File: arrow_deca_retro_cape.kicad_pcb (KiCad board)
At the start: 2 copper layers, 100 x 100 mm, 78 parts, among them J1 DB15_Female_HighDensity_Mount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, J10 Conn_02x06_Odd_Even, J11 PMOD1, J12 PMOD2, J14 Conn_01x02, J15 Conn_01x03, J16 Conn_01x06, J17 Conn_01x02, J18 Conn_01x03, J19 DINC_MIN_TM_6_1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

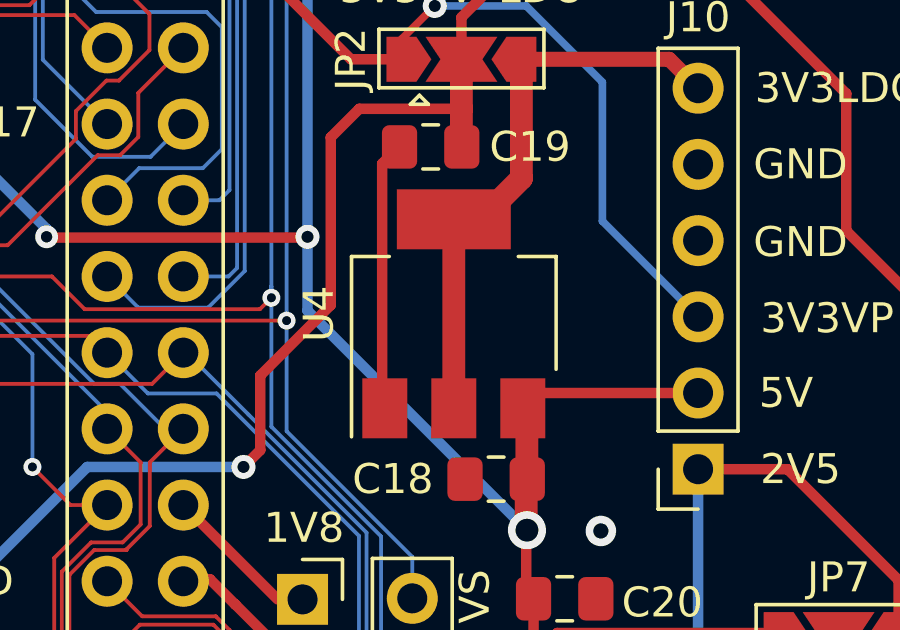
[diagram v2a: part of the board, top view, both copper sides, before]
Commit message: v0.83 Added jlcpcb parts with jlcpcb tools plugin
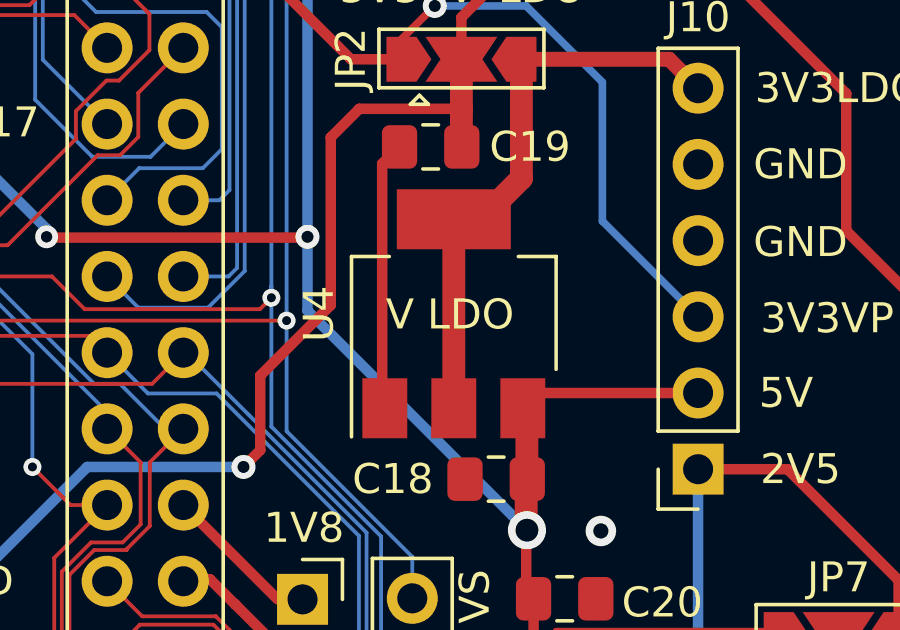
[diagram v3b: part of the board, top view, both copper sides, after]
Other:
- board text added: "V LDO"
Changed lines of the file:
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@@
     (property "Sheetfile" "arrow_deca_retro_cape.kicad_sch")
     (property "Sheetname" "")
-    (attr through_hole)
+    (attr through_hole exclude_from_pos_files exclude_from_bom)
     (fp_text reference "J9" (at 1.283 -2.9718 180) (layer "F.SilkS")
       (effects (font (size 1 1) (thickness 0.15)))
@@
     (property "Sheetfile" "arrow_deca_retro_cape.kicad_sch")
     (property "Sheetname" "")
-    (attr through_hole)
+    (attr through_hole exclude_from_pos_files exclude_from_bom)
     (fp_text reference "J8" (at 1.156 -2.9718) (layer "F.SilkS")
       (effects (font (size 1 1) (thickness 0.15)))
@@
     (property "Sheetfile" "arrow_deca_retro_cape.kicad_sch")
     (property "Sheetname" "")
-    (attr smd)
+    (attr smd exclude_from_pos_files exclude_from_bom)
     (fp_text reference "U4" (at 0 -4.5 90) (layer "F.SilkS")
       (effects (font (size 1 1) (thickness 0.15)))
@@
     (property "Sheetfile" "arrow_deca_retro_cape.kicad_sch")
     (property "Sheetname" "")
-    (attr through_hole)
+    (attr through_hole exclude_from_pos_files exclude_from_bom)
     (fp_text reference "J20" (at -0.923331 15.315 -180) (layer "F.SilkS") hide
       (effects (font (size 1 1) (thickness 0.15)))
@@
     (property "Sheetfile" "arrow_deca_retro_cape.kicad_sch")
     (property "Sheetname" "")
-    (attr through_hole)
+    (attr through_hole exclude_from_pos_files exclude_from_bom)
     (fp_text reference "JP5" (at 0 -2.33) (layer "F.SilkS")
       (effects (font (size 1 1) (thickness 0.15)))
@@
     (property "Sheetfile" "arrow_deca_retro_cape.kicad_sch")
     (property "Sheetname" "")
-    (attr through_hole)
+    (attr through_hole exclude_from_pos_files exclude_from_bom)
     (fp_text reference "J2" (at 0 -2.286 180) (layer "F.SilkS")
       (effects (font (size 1 1) (thickness 0.15)))
@@
     (property "Sheetfile" "arrow_deca_retro_cape.kicad_sch")
     (property "Sheetname" "")
-    (attr through_hole)
+    (attr through_hole exclude_from_pos_files exclude_from_bom)
     (fp_text reference "J16" (at 0 -2.77 180) (layer "F.SilkS")
       (effects (font (size 1 1) (thickness 0.15)))
@@
     (property "Sheetfile" "arrow_deca_retro_cape.kicad_sch")
     (property "Sheetname" "")
-    (attr exclude_from_pos_files)
+    (attr exclude_from_pos_files exclude_from_bom)
     (fp_text reference "JP2" (at -3.683 0 90) (layer "F.SilkS")
       (effects (font (size 1 1) (thickness 0.15)))
@@
     (property "Sheetfile" "arrow_deca_retro_cape.kicad_sch")
     (property "Sheetname" "")
-    (attr through_hole)
+    (attr through_hole exclude_from_pos_files exclude_from_bom)
     (fp_text reference "JP8" (at 0 -2.33 90) (layer "F.SilkS")
       (effects (font (size 1 1) (thickness 0.15)))
@@
     (property "Sheetfile" "arrow_deca_retro_cape.kicad_sch")
     (property "Sheetname" "")
-    (attr smd)
+    (attr smd exclude_from_pos_files exclude_from_bom)
     (fp_text reference "R3" (at -2.908 0) (layer "F.SilkS")
       (effects (font (size 1 1) (thickness 0.15)))
@@
     (property "Sheetfile" "arrow_deca_retro_cape.kicad_sch")
     (property "Sheetname" "")
-    (attr through_hole)
+    (attr through_hole exclude_from_pos_files exclude_from_bom)
     (fp_text reference "J10" (at 0 15.061 180) (layer "F.SilkS")
       (effects (font (size 1 1) (thickness 0.15)))
@@
     (property "Sheetfile" "arrow_deca_retro_cape.kicad_sch")
     (property "Sheetname" "")
-    (attr through_hole)
+    (attr through_hole exclude_from_pos_files exclude_from_bom)
     (fp_text reference "J11" (at -1.27 -2.77 90) (layer "F.SilkS") hide
       (effects (font (size 1 1) (thickness 0.15)))
@@
     (property "Sheetfile" "arrow_deca_retro_cape.kicad_sch")
     (property "Sheetname" "")
-    (attr through_hole)
+    (attr through_hole exclude_from_pos_files exclude_from_bom)
     (fp_text reference "JP4" (at 0 -2.33) (layer "F.SilkS")
       (effects (font (size 1 1) (thickness 0.15)))
@@
     (property "Sheetfile" "arrow_deca_retro_cape.kicad_sch")
     (property "Sheetname" "")
+    (attr exclude_from_pos_files exclude_from_bom)
     (fp_text reference "J5" (at -7.5596 12.827 90) (layer "F.SilkS")
       (effects (font (size 1 1) (thickness 0.15)) (justify left bottom))
@@
     (property "Sheetfile" "arrow_deca_retro_cape.kicad_sch")
     (property "Sheetname" "")
-    (attr exclude_from_pos_files)
+    (attr exclude_from_pos_files exclude_from_bom)
     (fp_text reference "JP3" (at -0.142 2.032 90 unlocked) (layer "F.SilkS")
       (effects (font (size 1 1) (thickness 0.15)))
@@
     (property "Sheetfile" "arrow_deca_retro_cape.kicad_sch")
     (property "Sheetname" "")
-    (attr through_hole)
+    (attr through_hole exclude_from_pos_files exclude_from_bom)
     (fp_text reference "J1" (at -4.315 -2.61 -90) (layer "F.SilkS") hide
       (effects (font (size 1 1) (thickness 0.15)))
@@
     (property "Sheetfile" "arrow_deca_retro_cape.kicad_sch")
     (property "Sheetname" "")
-    (attr smd)
+    (attr smd exclude_from_pos_files exclude_from_bom)
     (fp_text reference "U5" (at 0.4814 -4.243469 -90) (layer "F.SilkS")
       (effects (font (size 1 1) (thickness 0.15)))
@@
     (property "Sheetfile" "arrow_deca_retro_cape.kicad_sch")
     (property "Sheetname" "")
-    (attr smd)
+    (attr smd exclude_from_pos_files exclude_from_bom)
     (fp_text reference "R4" (at -2.908 0) (layer "F.SilkS")
       (effects (font (size 1 1) (thickness 0.15)))
@@
     (property "Sheetfile" "arrow_deca_retro_cape.kicad_sch")
     (property "Sheetname" "")
-    (attr exclude_from_pos_files)
+    (attr exclude_from_pos_files exclude_from_bom)
     (fp_text reference "JP7" (at 0 -1.905) (layer "F.SilkS")
       (effects (font (size 1 1) (thickness 0.15)))
@@
     (property "Sheetfile" "arrow_deca_retro_cape.kicad_sch")
     (property "Sheetname" "")
-    (attr through_hole)
+    (attr through_hole exclude_from_pos_files exclude_from_bom)
     (fp_text reference "J3" (at -0.0508 -2.286 180) (layer "F.SilkS")
       (effects (font (size 1 1) (thickness 0.15)))
@@
     (property "Sheetfile" "arrow_deca_retro_cape.kicad_sch")
     (property "Sheetname" "")
-    (attr through_hole)
+    (attr through_hole exclude_from_pos_files exclude_from_bom)
     (fp_text reference "J14" (at -0.025 6.33) (layer "F.SilkS")
       (effects (font (size 1 1) (thickness 0.15)))
@@
     (property "Sheetfile" "arrow_deca_retro_cape.kicad_sch")
     (property "Sheetname" "")
+    (attr exclude_from_pos_files exclude_from_bom)
     (fp_text reference "J19" (at -7.5946 12.827 90) (layer "F.SilkS")
       (effects (font (size 1 1) (thickness 0.15)) (justify left bottom))
@@
     (property "Sheetfile" "arrow_deca_retro_cape.kicad_sch")
     (property "Sheetname" "")
-    (attr through_hole)
+    (attr through_hole exclude_from_pos_files exclude_from_bom)
     (fp_text reference "J15" (at 0 -2.33 90) (layer "F.SilkS")
       (effects (font (size 1 1) (thickness 0.15)))
@@
     (property "Sheetfile" "arrow_deca_retro_cape.kicad_sch")
     (property "Sheetname" "")
-    (attr through_hole)
+    (attr through_hole exclude_from_pos_files exclude_from_bom)
     (fp_text reference "J4" (at 22.112 -1.221669) (layer "F.SilkS")
       (effects (font (size 1 1) (thickness 0.15)))
@@
     (property "Sheetfile" "arrow_deca_retro_cape.kicad_sch")
     (property "Sheetname" "")
-    (attr through_hole)
+    (attr through_hole exclude_from_pos_files exclude_from_bom)
     (fp_text reference "J18" (at 0 -2.301) (layer "F.SilkS")
       (effects (font (size 1 1) (thickness 0.15)))
@@
     (property "Sheetfile" "arrow_deca_retro_cape.kicad_sch")
     (property "Sheetname" "")
-    (attr through_hole)
+    (attr through_hole exclude_from_pos_files exclude_from_bom)
     (fp_text reference "JP6" (at 0 -2.33) (layer "F.SilkS")
       (effects (font (size 1 1) (thickness 0.15)))
@@
     (property "Sheetfile" "arrow_deca_retro_cape.kicad_sch")
     (property "Sheetname" "")
-    (attr through_hole)
+    (attr through_hole exclude_from_pos_files exclude_from_bom)
     (fp_text reference "J17" (at 0.0508 6.8326 180) (layer "F.SilkS")
       (effects (font (size 1 1) (thickness 0.15)))
@@
     (property "Sheetfile" "arrow_deca_retro_cape.kicad_sch")
     (property "Sheetname" "")
-    (attr through_hole)
+    (attr through_hole exclude_from_pos_files exclude_from_bom)
     (fp_text reference "J22" (at 0 -2.33) (layer "F.SilkS")
       (effects (font (size 1 1) (thickness 0.15)))
@@
     (property "Sheetfile" "arrow_deca_retro_cape.kicad_sch")
     (property "Sheetname" "")
-    (attr through_hole)
+    (attr through_hole exclude_from_pos_files exclude_from_bom)
     (fp_text reference "J12" (at -1.27 -2.77 90) (layer "F.SilkS") hide
       (effects (font (size 1 1) (thickness 0.15)))
@@
     (property "Sheetfile" "arrow_deca_retro_cape.kicad_sch")
     (property "Sheetname" "")
-    (attr through_hole)
+    (attr through_hole exclude_from_pos_files exclude_from_bom)
     (fp_text reference "JP1" (at -2.159 1.143 -180) (layer "F.SilkS")
       (effects (font (size 1 1) (thickness 0.15)))
@@
     (property "Sheetfile" "arrow_deca_retro_cape.kicad_sch")
     (property "Sheetname" "")
-    (attr through_hole)
+    (attr through_hole exclude_from_pos_files exclude_from_bom)
     (fp_text reference "J7" (at 0 7.685) (layer "F.SilkS")
       (effects (font (size 1 1) (thickness 0.15)))
@@
     (property "Sheetfile" "arrow_deca_retro_cape.kicad_sch")
     (property "Sheetname" "")
-    (attr through_hole)
+    (attr through_hole exclude_from_pos_files exclude_from_bom)
     (fp_text reference "J6" (at 1.27 50.8) (layer "F.SilkS")
       (effects (font (size 1 1) (thickness 0.15)))
@@
     (effects (font (size 1 1) (thickness 0.15)))
   )
+  (gr_text "V LDO" (at 128.27 77.47) (layer "F.SilkS")
+    (effects (font (size 1 1) (thickness 0.15)))
+  )

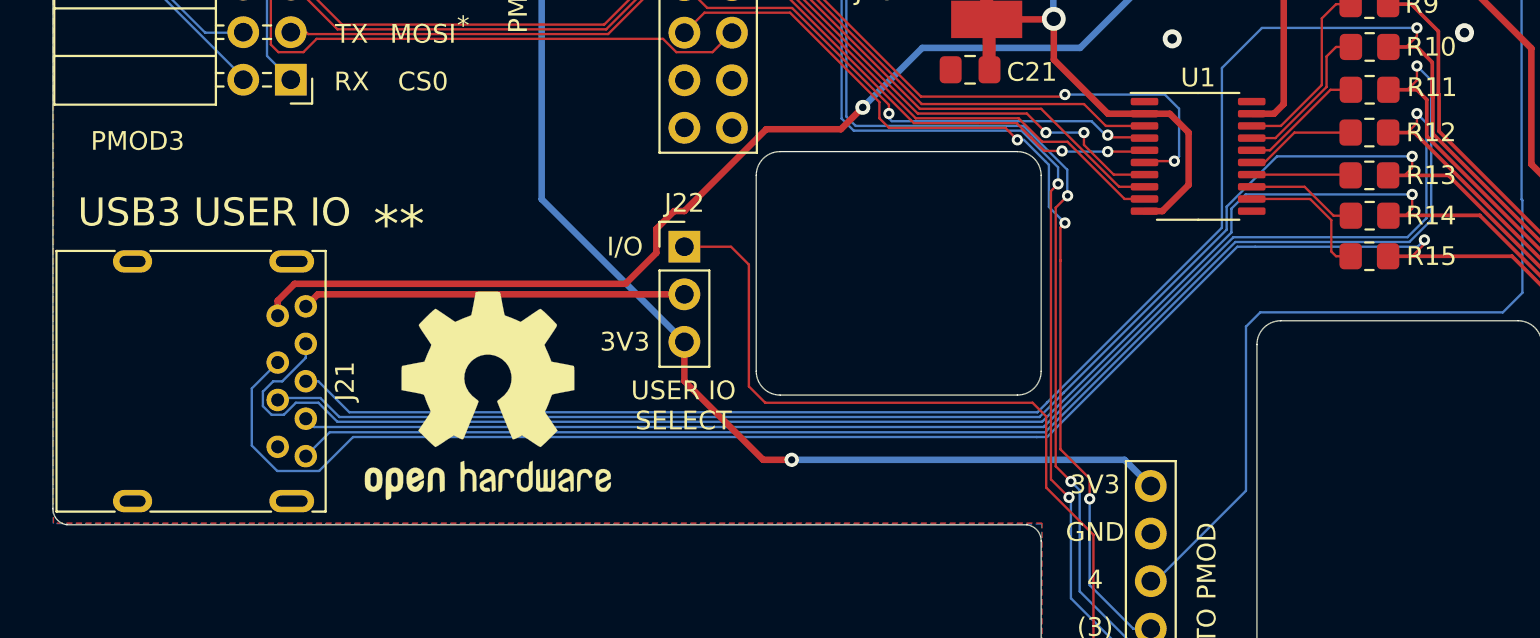
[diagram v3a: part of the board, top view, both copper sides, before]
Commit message: v0.84 updated USB3 footprint
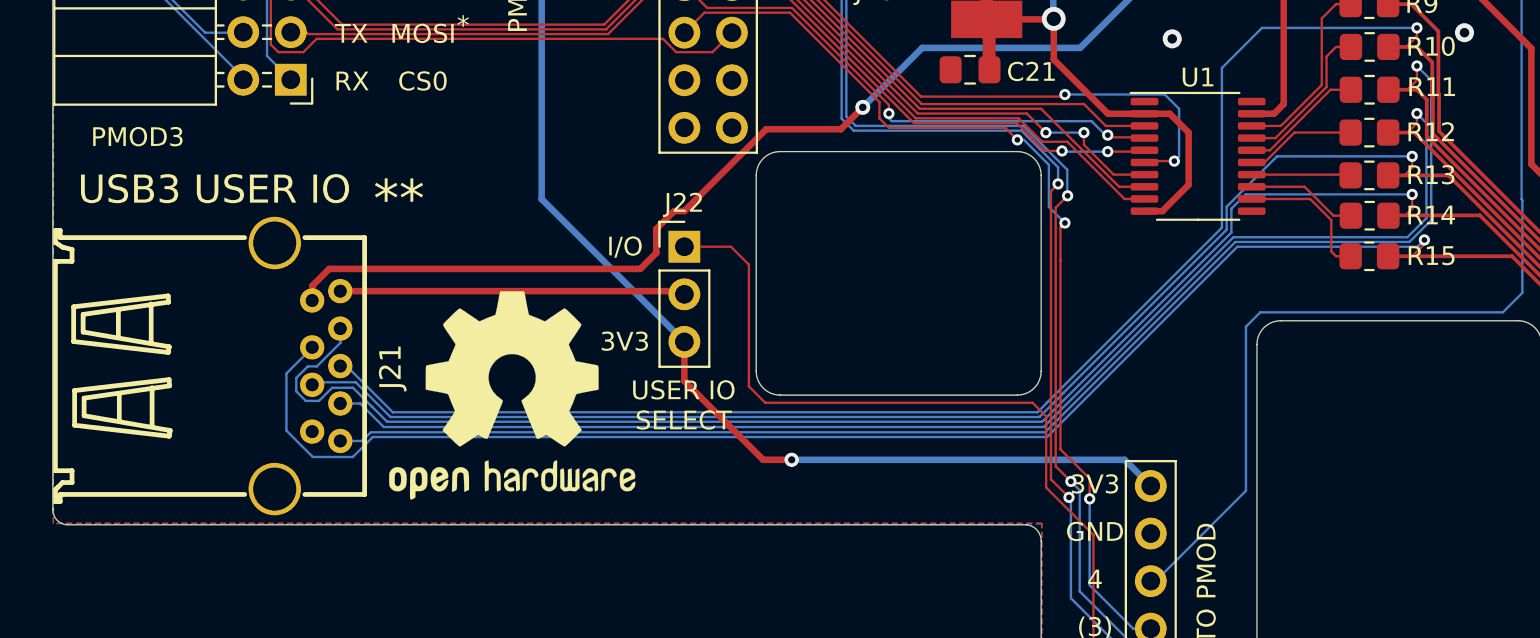
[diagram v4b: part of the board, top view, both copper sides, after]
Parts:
- J21: footprint Connector_USB:USB3_A_Molex_48393-001 -> varis:USB-3.0-TH_C69073
- moved J21 3.12 mm to (96.7, 114.3)
- moved LO2 1.30 mm to (107.6, 115.9)
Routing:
- net /+JOY_PWR_USB3: track 63.8 -> 61.6 mm
- net /D-: track 108.2 -> 106.0 mm
- net /RX-: track 111.2 -> 109.2 mm
- net /TX+: track 20.5 -> 18.4 mm
- net /RX+: track 108.9 -> 107.4 mm
- net /DRAIN: track 112.9 -> 111.4 mm
- net /D+: track 102.7 -> 101.2 mm
- net /TX-: track 110.3 -> 108.9 mm
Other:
- outline, holes or cut-outs redrawn
